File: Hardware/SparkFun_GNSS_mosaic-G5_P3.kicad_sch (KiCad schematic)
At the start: 65 parts, among them J1 USB_C_Receptacle, J10 U.FL, J2 Conn_01x06, J4 Conn_01x10, J5 SMA_Edge, J6 Conn_01x11, J8 JST_Locking_4, U1 DT1042-04SO, U2 RT9080-3.3, U3 mosaic-G5 P3

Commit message: Ready for protos
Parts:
- removed C2: 10uF, SparkFun-Capacitor:C_0603_1608Metric, symbol SparkFun-Capacitor:10uF_0603_6.3V_20%
- added C14: 1.0uF, SparkFun-Capacitor:C_0603_1608Metric, symbol SparkFun-Capacitor:1.0uF_0603_16V_10%
- C3: value 10uF -> 22uF; symbol SparkFun-Capacitor:10uF_0603_6.3V_20% -> SparkFun-Capacitor:22uF_0603_6.3V_20%; PROD_ID CAP-11015 -> CAP-14464
- TP1, TP3, TP4, TP5: value 1.25mm -> 1.0mm
- U3: PROD_ID (none) -> IC-26406
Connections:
- net 3.3V: now also C14.1
- net GND: now also C14.2
- net USB_D+: no longer TP3.1
- net USB_D-: no longer TP4.1
- net at J1.A7 (D-), J1.B7 (D-), TR1.1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: now also TP4.1
- net at J1.A6 (D+), J1.B6 (D+), TR1.3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: now also TP3.1
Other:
- moved on the sheet: TP3, TP4

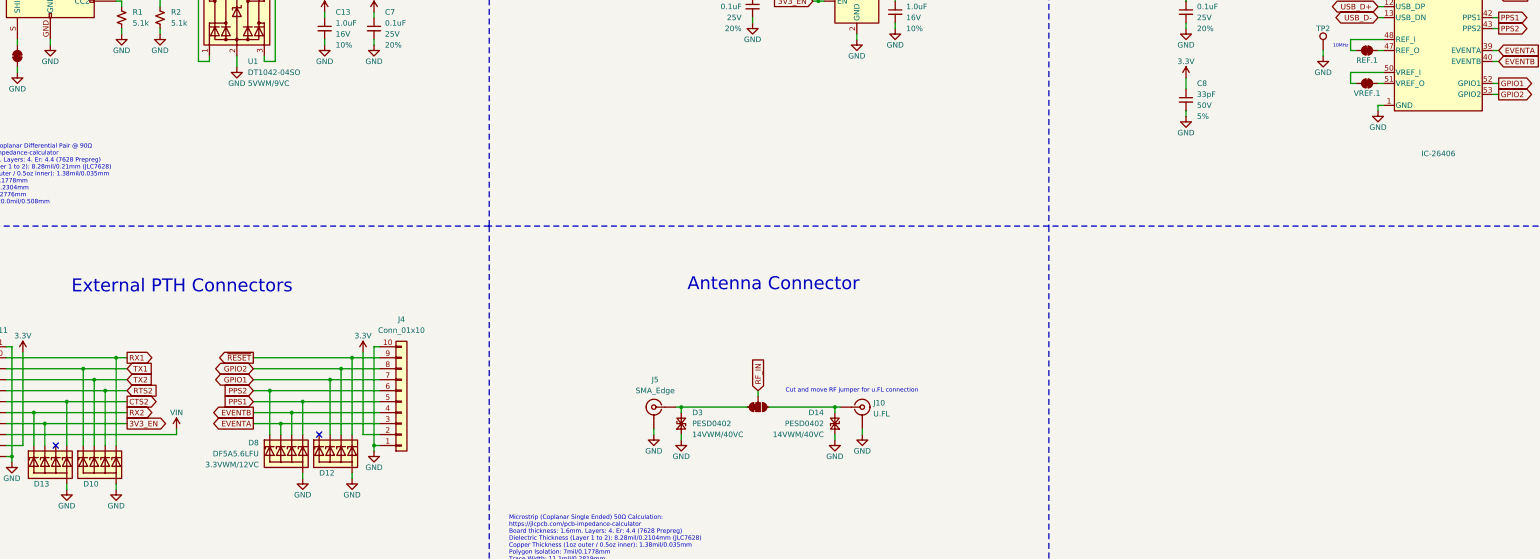
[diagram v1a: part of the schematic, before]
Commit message: Re-panelized with paste reduction
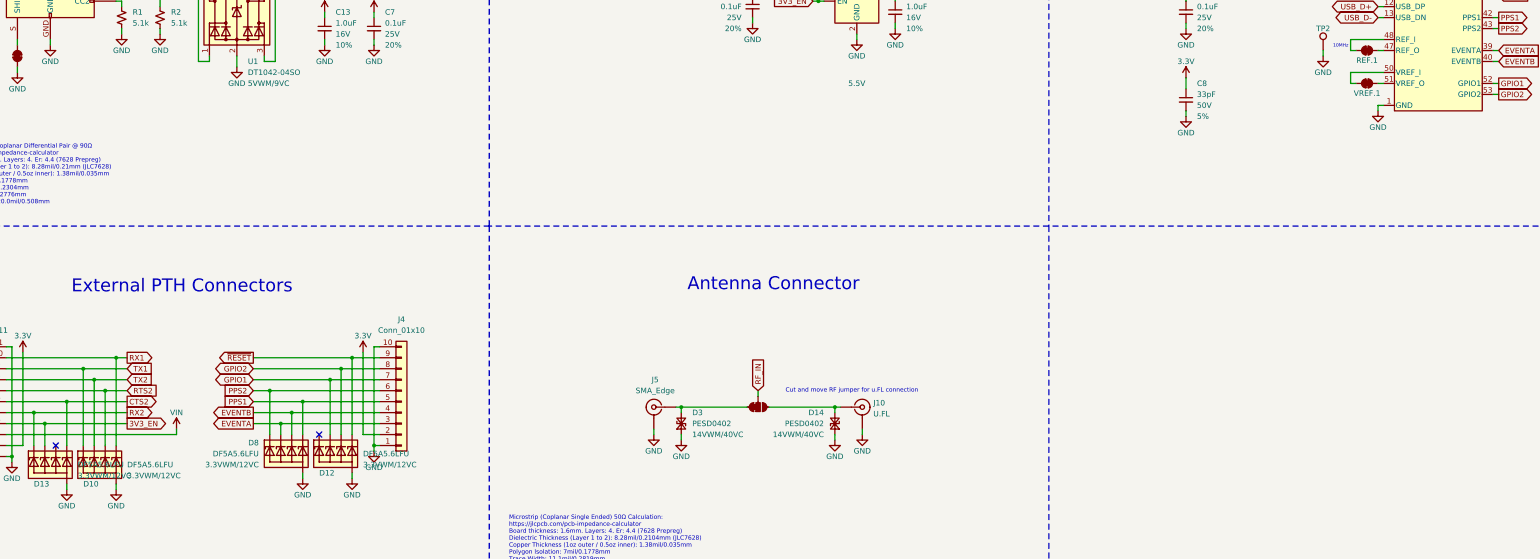
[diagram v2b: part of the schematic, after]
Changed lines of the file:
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@@
 					(size 1.27 1.27)
 				)
-				(hide yes)
 			)
 		)
@@
 				)
 				(justify left)
-				(hide yes)
 			)
 		)
@@
 				)
 				(justify left)
-				(hide yes)
 			)
 		)
@@
 					(size 1.27 1.27)
 				)
+				(hide yes)
 			)
 		)
@@
 		(pin "26"
 		)
+		(pin "8"
+		)
+		(pin "16"
+		)
+		(pin "24"
+		)
+		(pin "15"
+		)
+		(pin "36"
+		)
+		(pin "23"
+		)
+		(pin "35"
+		)
+		(pin "18"
+		)
+		(pin "19"
+		)
+		(pin "22"
+		)
+		(pin "20"
+		)
+		(pin "30"
+		)
+		(pin "32"
+		)
+		(pin "33"
+		)
+		(pin "31"
+		)
+		(pin "37"
+		)
+		(pin "38"
+		)
 		(instances
 			(project ""
@@
 				)
 				(justify left)
-				(hide yes)
 			)
 		)
@@
 				)
 				(justify left)
-				(hide yes)
 			)
 		)
@@
 				)
 				(justify left)
-				(hide yes)
 			)
 		)
@@
 				)
 				(justify left)
-				(hide yes)
 			)
 		)

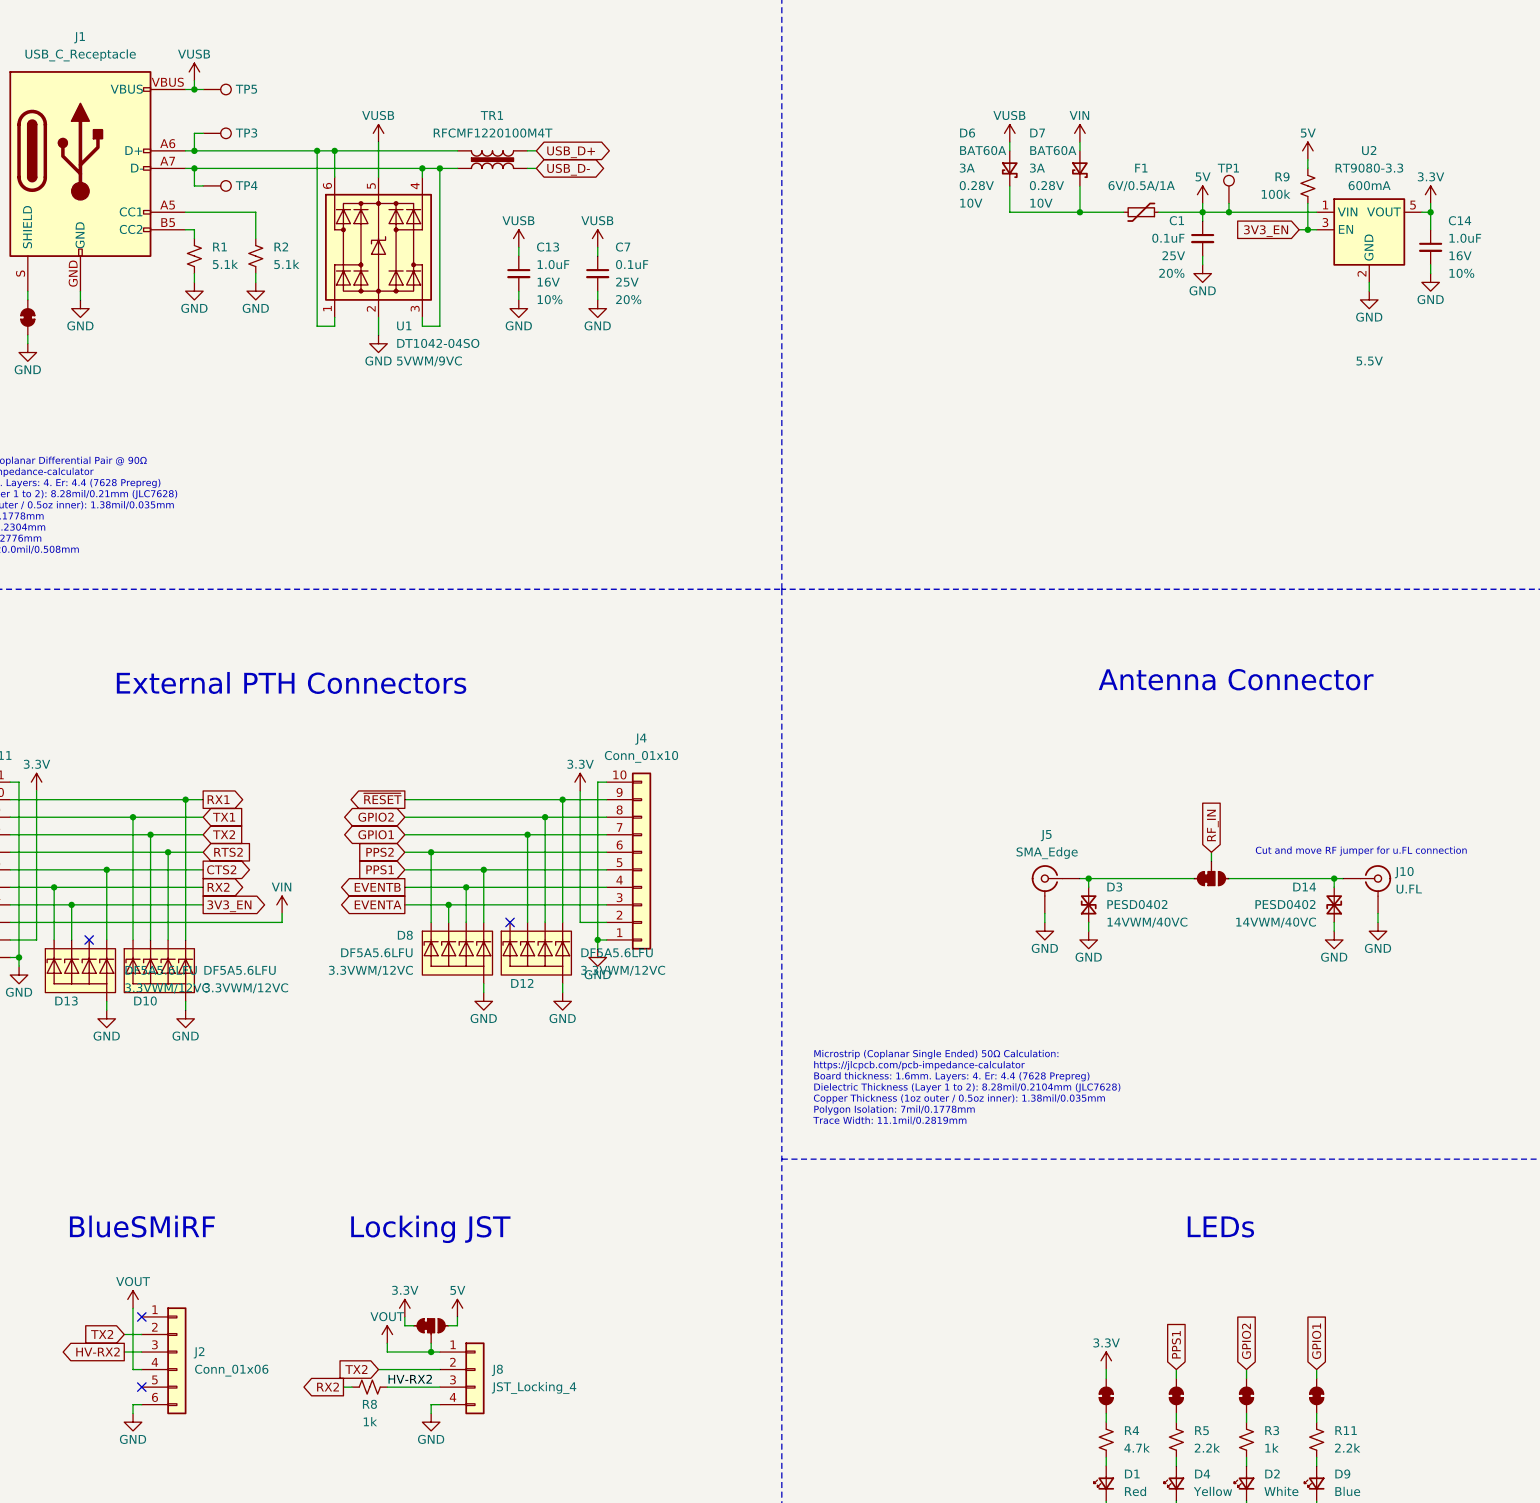
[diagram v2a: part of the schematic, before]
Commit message: Update symbols and 3D models
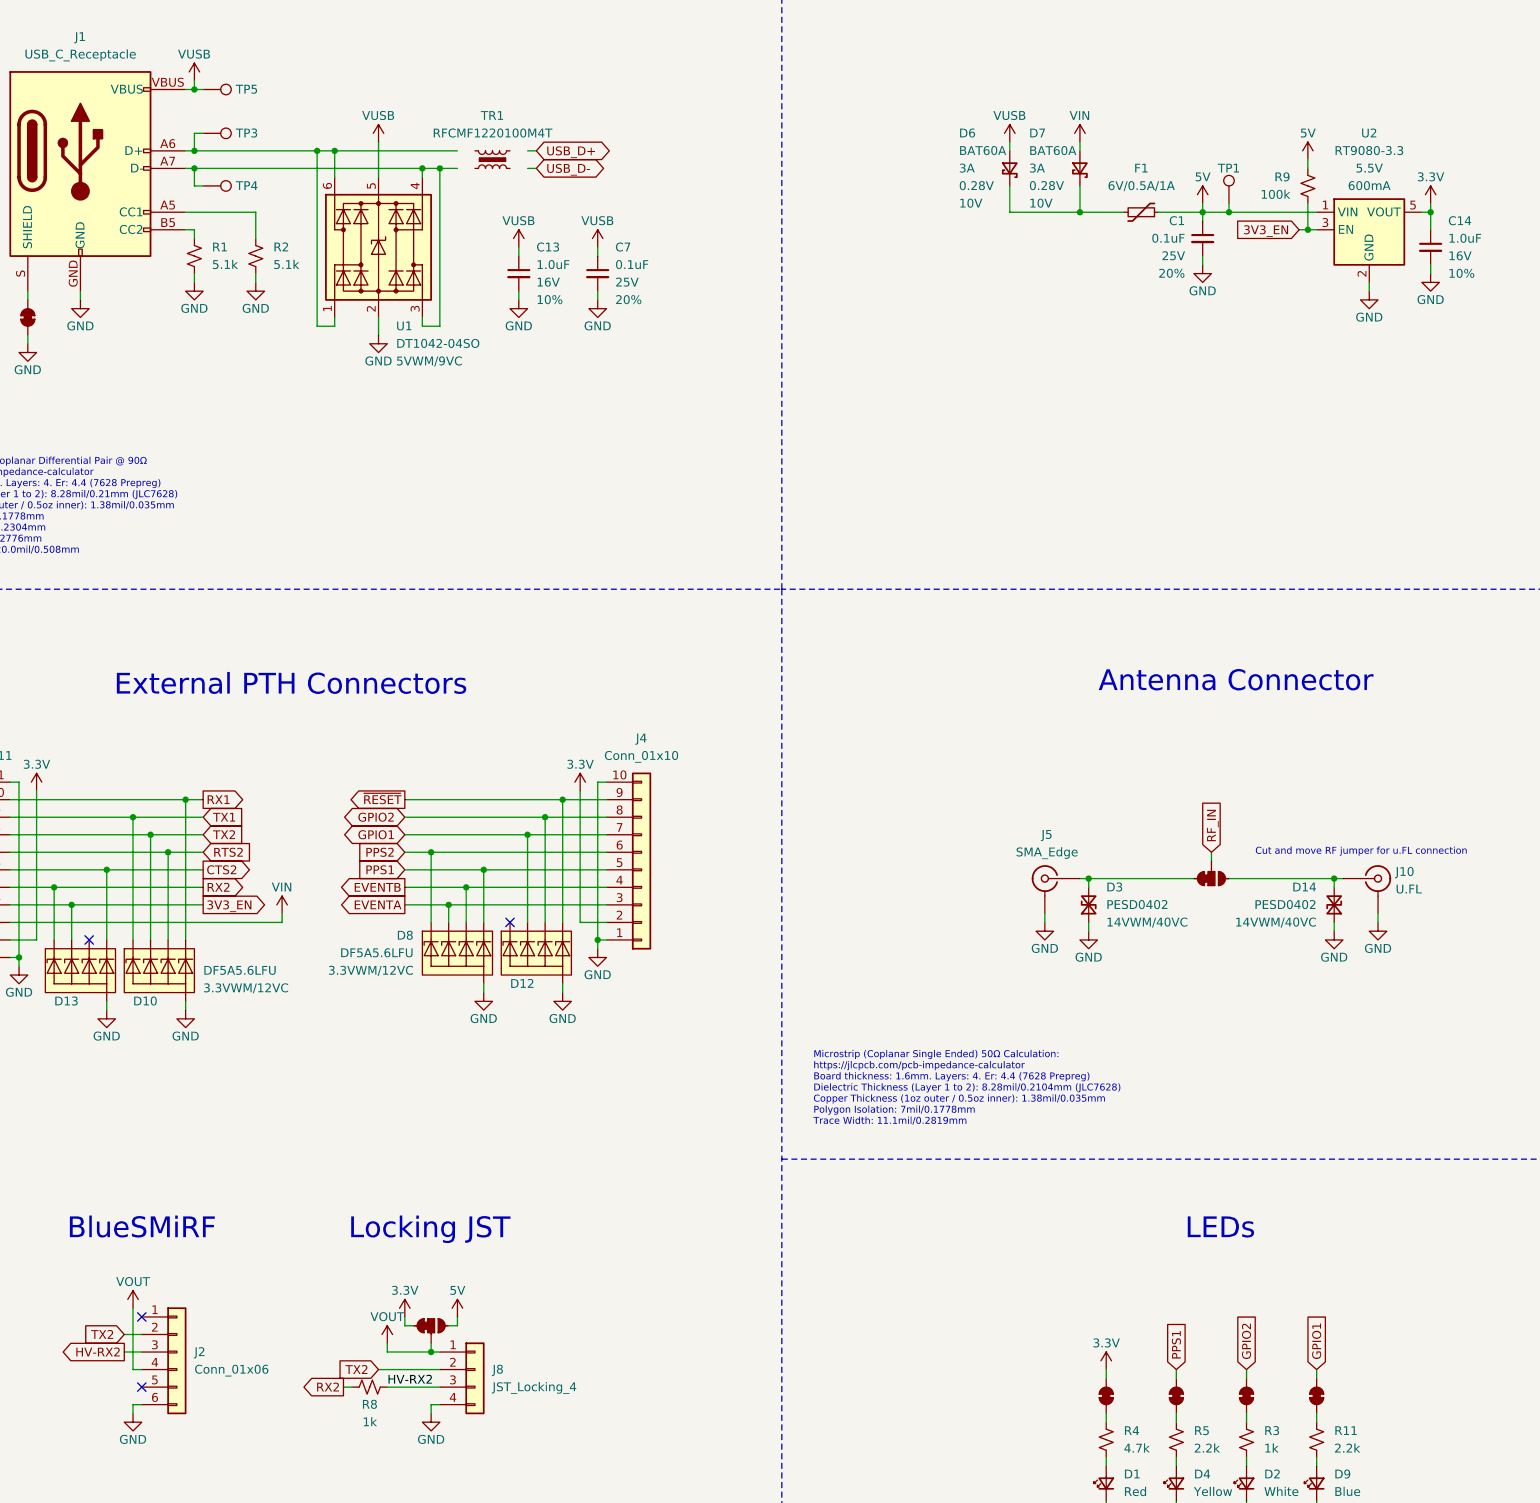
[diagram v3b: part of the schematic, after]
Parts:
- J2: footprint SparkFun-Connector:1x06 -> SparkFun-Connector:1x06_P2.54mm; symbol SparkFun-Connector:Conn_01x06 -> SparkFun-Connector:Conn_01x06_P2.54mm
- J4: footprint SparkFun-Connector:1x10 -> SparkFun-Connector:1x10_P2.54mm; symbol SparkFun-Connector:Conn_01x10 -> SparkFun-Connector:Conn_01x10_P2.54mm
- J5: footprint SparkFun-Connector:SMA_Edge -> SparkFun-Connector:SMA_Edge_6.3mm; symbol SparkFun-RF:SMA_EdgeMount -> SparkFun-RF:SMA_EdgeMount_6.3mm
- J6: footprint SparkFun-Connector:1x11 -> SparkFun-Connector:1x11_P2.54mm; symbol SparkFun-Connector:Conn_01x11 -> SparkFun-Connector:Conn_01x11_P2.54mm
- J8: footprint SparkFun-Connector:JST_SMD_1.25mm-4_Locking -> SparkFun-Connector:JST_1x04_P1.25mm_Locking_Horizontal_SMD; symbol SparkFun-Connector:Conn_01x04_JST_1.25mm_Locking -> SparkFun-Connector:Conn_01x04_JST_P1.25mm_Locking_Horizontal_SMD
- TR1: footprint SparkFun-Coil:RFCMF1220100M4T -> SparkFun-Coil:Choke_100MHz_USB
- U3: footprint SparkFun-CustomParts:MOSAIC-G5_LGA54 -> SparkFun-GPS:MOSAIC-G5_LGA54; symbol SparkFun-CustomParts:mosaic-G5_P3 -> SparkFun-GPS:mosaic-G5_P3
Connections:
- net USB_D+: no longer TR1.4
- net USB_D-: no longer TR1.2
- net at J1.A7 (D-), J1.B7 (D-), TP4.1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: no longer TR1.1
- net at J1.A6 (D+), J1.B6 (D+), TP3.1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: no longer TR1.3
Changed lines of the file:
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@@
 	)
 	(symbol
-		(lib_id "SparkFun-RF:SMA_EdgeMount")
+		(lib_id "SparkFun-RF:SMA_EdgeMount_6.3mm")
 		(at 185.42 154.94 0)
 		(mirror y)
@@
 			)
 		)
-		(property "Footprint" "SparkFun-Connector:SMA_Edge"
+		(property "Footprint" "SparkFun-Connector:SMA_Edge_6.3mm"
 			(at 185.42 165.1 0)
 			(effects
@@
 			)
 		)
-		(property "Datasheet" "https://www.sparkfun.com/datasheets/Wireless/Antenna/SMA-Connector.pdf"
+		(property "Datasheet" "https://cdn.sparkfun.com/assets/4/1/2/2/0/SMA-Connector.pdf"
 			(at 185.42 167.64 0)
 			(effects
@@
 			)
 		)
-		(property "Description" "SMA PCB Edge Mount connector"
+		(property "Description" "Not for new designs. Use 8mm variant. SMA PCB Edge Mount connector"
 			(at 185.42 170.18 0)
 			(effects
@@
 	)
 	(symbol
-		(lib_id "SparkFun-Connector:Conn_01x04_JST_1.25mm_Locking")
+		(lib_id "SparkFun-Connector:Conn_01x04_JST_P1.25mm_Locking_Horizontal_SMD")
 		(at 102.87 226.06 0)
 		(unit 1)
@@
 			)
 		)
-		(property "Footprint" "SparkFun-Connector:JST_SMD_1.25mm-4_Locking"
+		(property "Footprint" "SparkFun-Connector:JST_1x04_P1.25mm_Locking_Horizontal_SMD"
 			(at 102.87 236.22 0)
 			(effects
@@
 		(on_board yes)
 		(dnp no)
-		(fields_autoplaced yes)
 		(property "Reference" "U2"
-			(at 232.41 49.53 0)
+			(at 232.41 46.99 0)
 			(effects
 				(font
@@
 		)
 		(property "Value" "RT9080-3.3"
-			(at 232.41 52.07 0)
+			(at 232.41 49.53 0)
 			(effects
 				(font
@@
 		)
 		(property "VMax" "5.5V"
-			(at 232.41 80.01 0)
+			(at 232.41 52.07 0)
 			(effects
 				(font
@@
 	)
 	(symbol
-		(lib_id "SparkFun-CustomParts:mosaic-G5_P3")
+		(lib_id "SparkFun-GPS:mosaic-G5_P3")
 		(at 367.03 62.23 0)
 		(unit 1)
@@
 			)
 		)
-		(property "Footprint" "SparkFun-CustomParts:MOSAIC-G5_LGA54"
+		(property "Footprint" "SparkFun-GPS:MOSAIC-G5_LGA54"
 			(at 367.03 91.948 0)
 			(effects
@@
 			)
 		)
-		(property "Datasheet" "https://docs.broadcom.com/docs/AV02-0551EN"
+		(property "Datasheet" "https://www.kingbrightusa.com/images/catalog/SPEC/APT1608SURCK.pdf"
 			(at 194.31 242.57 0)
 			(effects
@@
 				)
 				(justify left)
+				(hide yes)
 			)
 		)
@@
 				)
 				(justify left)
+				(hide yes)
 			)
 		)
@@
 			)
 		)
-		(property "Footprint" "SparkFun-Coil:RFCMF1220100M4T"
+		(property "Footprint" "SparkFun-Coil:Choke_100MHz_USB"
 			(at 104.14 44.45 0)
 			(effects
@@
 		(pin "2"
 		)
-		(pin "3"
+		(pin "1"
 		)
-		(pin "4"
+		(pin "2"
 		)
 		(instances
@@
 	)
 	(symbol
-		(lib_id "SparkFun-Connector:Conn_01x11")
+		(lib_id "SparkFun-Connector:Conn_01x11_P2.54mm")
 		(at 30.48 153.67 180)
 		(unit 1)
@@
 			)
 		)
-		(property "Footprint" "SparkFun-Connector:1x11"
+		(property "Footprint" "SparkFun-Connector:1x11_P2.54mm"
 			(at 30.48 135.89 0)
 			(effects
@@
 	)
 	(symbol
-		(lib_id "SparkFun-Connector:Conn_01x06")
+		(lib_id "SparkFun-Connector:Conn_01x06_P2.54mm")
 		(at 59.69 223.52 0)
 		(unit 1)
@@
 		(fields_autoplaced yes)
 		(property "Reference" "J2"
-			(at 62.23 223.52 0)
+			(at 62.23 223.5199 0)
 			(effects
 				(font
@@
 		)
 		(property "Value" "Conn_01x06"
-			(at 62.23 226.06 0)
+			(at 62.23 226.0599 0)
 			(effects
 				(font
@@
 			)
 		)
-		(property "Footprint" "SparkFun-Connector:1x06"
-			(at 59.69 223.52 0)
+		(property "Footprint" "SparkFun-Connector:1x06_P2.54mm"
+			(at 59.69 236.22 0)
 			(effects
 				(font
@@
 		)
 		(property "Datasheet" "~"
-			(at 59.69 223.52 0)
+			(at 59.69 238.76 0)
 			(effects
 				(font
@@
 		)
 		(property "Description" "Basic 0.1\" PTH"
-			(at 59.69 223.52 0)
+			(at 59.69 241.3 0)
 			(effects
 				(font
@@
 	)
 	(symbol
-		(lib_id "SparkFun-Connector:Conn_01x10")
+		(lib_id "SparkFun-Connector:Conn_01x10_P2.54mm")
 		(at 127 153.67 0)
 		(mirror x)
@@
 			)
 		)
-		(property "Footprint" "SparkFun-Connector:1x10"
+		(property "Footprint" "SparkFun-Connector:1x10_P2.54mm"
 			(at 127 135.89 0)
 			(effects
@@
 				)
 				(justify left)
+				(hide yes)
 			)
 		)
@@
 				)
 				(justify left)
+				(hide yes)
 			)
 		)
